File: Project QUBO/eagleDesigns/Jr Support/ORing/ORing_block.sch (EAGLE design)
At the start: 73 parts

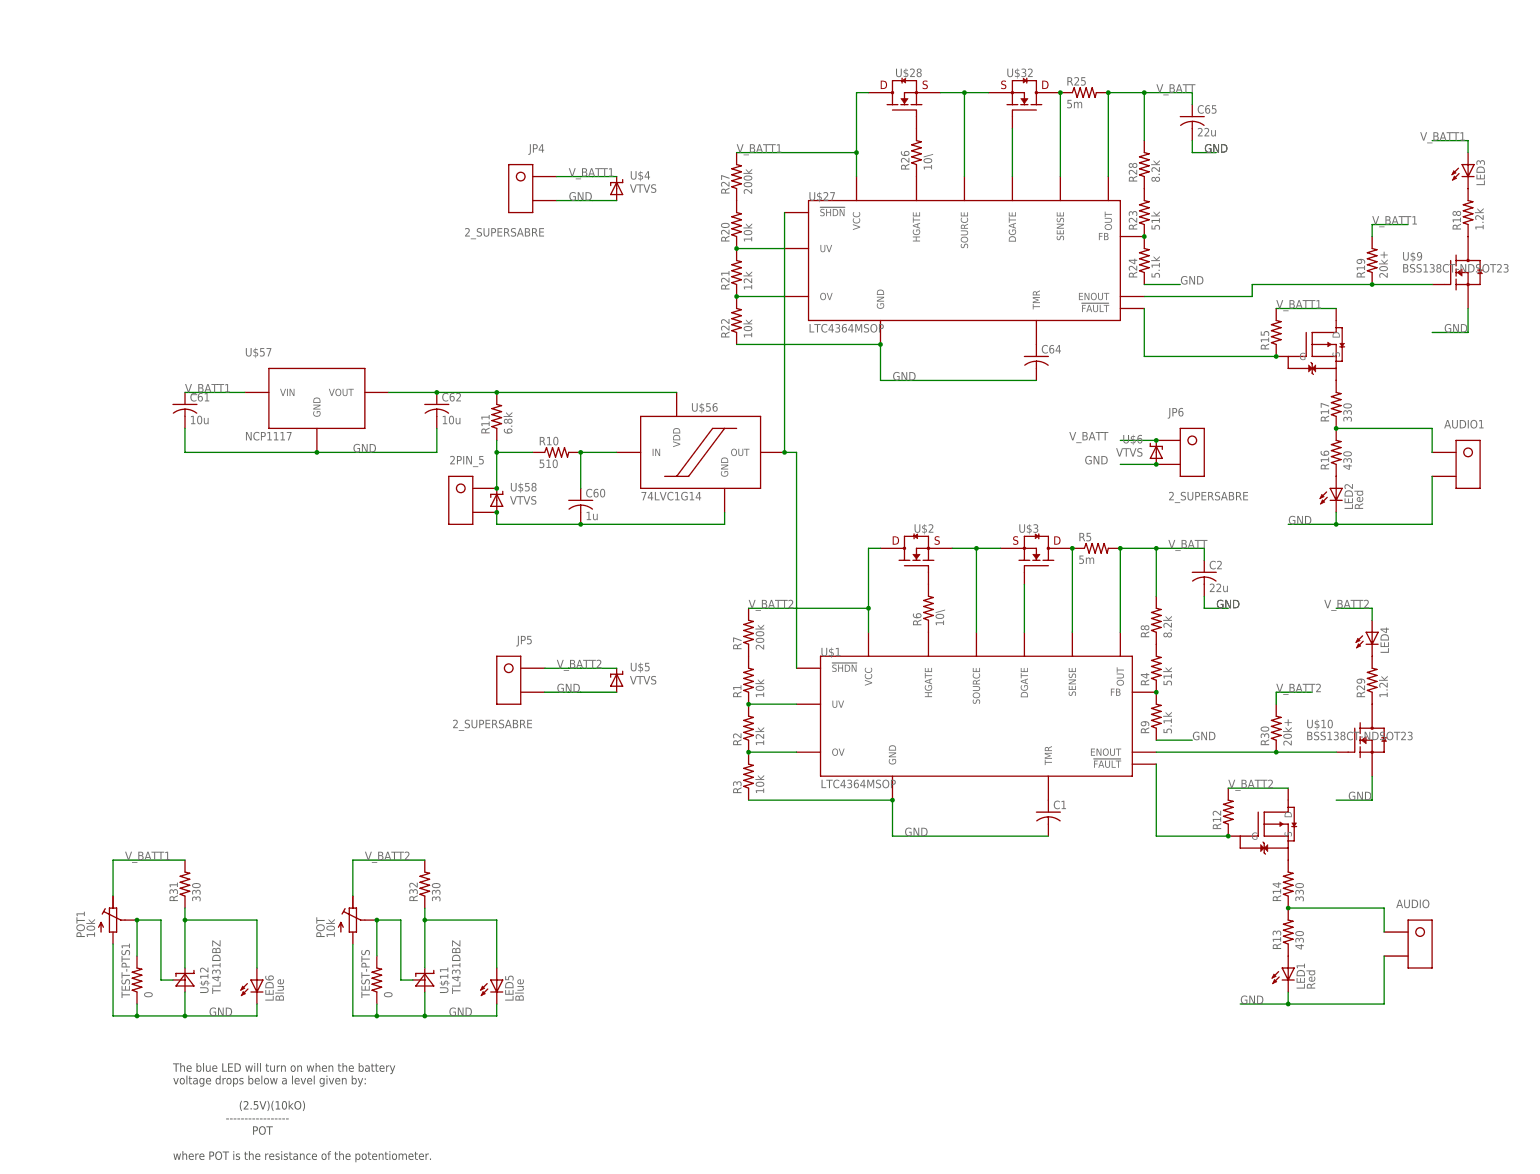
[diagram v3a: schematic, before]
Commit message: 
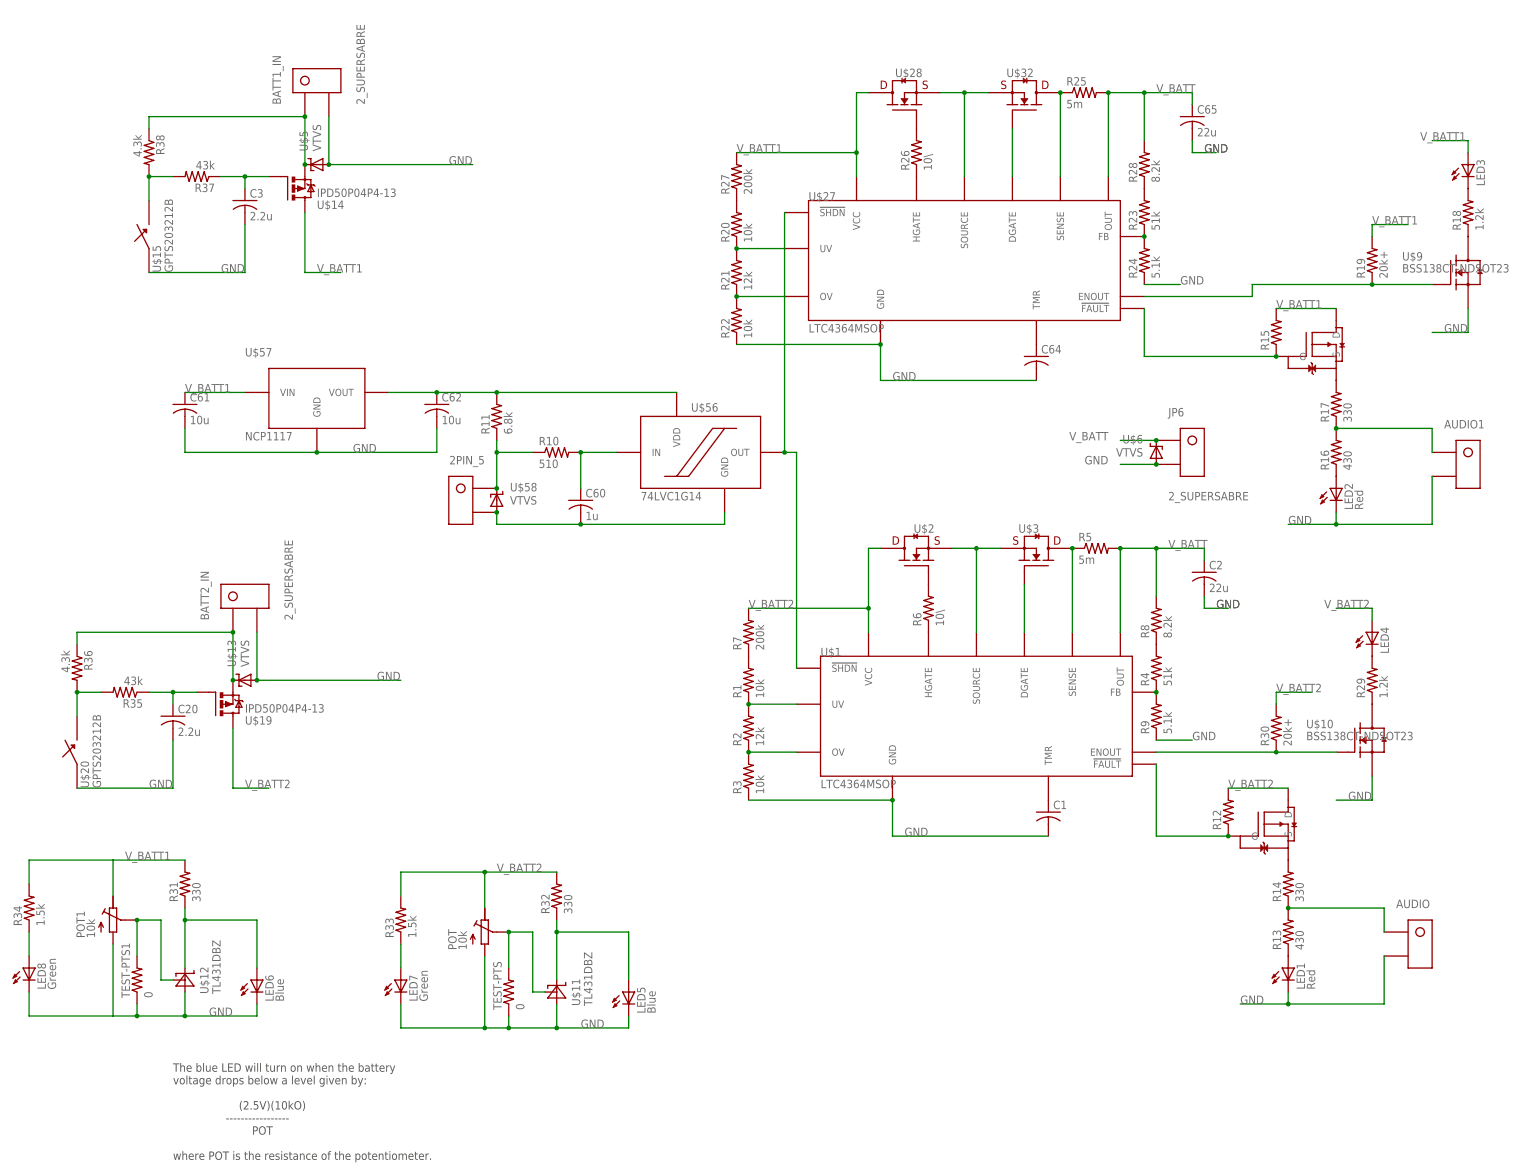
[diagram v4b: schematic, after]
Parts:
- removed JP4, JP5: 2_SUPERSABRE, molex:2_SUPERSABRE
- removed U$4: VTVS, diode:VTVS
- added BATT1_IN, BATT2_IN: 2_SUPERSABRE, molex:2_SUPERSABRE
- added C20, C3: 2.2u, resistor:C-USC0805
- added LED7, LED8: Green, led:0805_LED
- added R33, R34: 1.5k, resistor:R-US_R0805
- added R35, R37: 43k, resistor:R-US_R0805
- added R36, R38: 4.3k, resistor:R-US_R0805
- added U$13: VTVS, diode:VTVS
- added U$14, U$19: IPD50P04P4-13, transistor-power:IPD50P04P4-13
- added U$15, U$20: GPTS203212B, switches:GPTS203212B
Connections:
- new net GND1: LED8.C
- new net N$33: LED7.A, R33.1
- new net N$34: LED8.A, R34.1
- new net N$35: C20.1, R35.1, U$19.G
- new net N$36: R35.2, R36.2, U$20.P$2
- new net N$38: BATT1_IN.P$1, R38.1, U$14.D, U$5.C
- new net N$40: C3.1, R37.1, U$14.G
- new net N$41: R37.2, R38.2, U$15.P$2
- new net N$45: BATT2_IN.P$1, R36.1, U$13.C, U$19.D
- new net V_BATT3: R34.2
- net GND: now also BATT1_IN.P$2, BATT2_IN.P$2, C20.2, C3.2, LED7.C, U$13.A, U$15.P$1, U$20.P$1; no longer JP4.P$2, JP5.P$2, U$4.A
- net V_BATT1: now also U$14.S; no longer JP4.P$1, U$4.C
- net V_BATT2: now also R33.2, U$19.S; no longer JP5.P$1, U$5.C
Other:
- moved on the sheet: LED5, POT, R32, TEST-PTS, U$11, U$5

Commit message: 
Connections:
- removed net GND1: LED8.C
- removed net V_BATT3: R34.2
- net GND: now also LED8.C
- net V_BATT1: now also R34.2
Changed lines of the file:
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@@
 <label x="-157.48" y="-2.54" size="1.778" layer="95"/>
+</segment>
+<segment>
+<pinref part="LED8" gate="G$1" pin="C"/>
+<wire x1="-180.34" y1="-160.02" x2="-198.12" y2="-160.02" width="0.1524" layer="91"/>
+<wire x1="-198.12" y1="-160.02" x2="-198.12" y2="-154.94" width="0.1524" layer="91"/>
 </segment>
 </net>
@@
 <wire x1="-139.7" y1="-2.54" x2="-132.08" y2="-2.54" width="0.1524" layer="91"/>
 <label x="-137.16" y="-2.54" size="1.778" layer="95"/>
+</segment>
+<segment>
+<pinref part="R34" gate="G$1" pin="2"/>
+<wire x1="-198.12" y1="-132.08" x2="-198.12" y2="-127" width="0.1524" layer="91"/>
+<wire x1="-198.12" y1="-127" x2="-180.34" y2="-127" width="0.1524" layer="91"/>
 </segment>
 </net>
@@
 </segment>
 </net>
-<net name="GND1" class="0">
-<segment>
-<pinref part="LED8" gate="G$1" pin="C"/>
-<wire x1="-180.34" y1="-160.02" x2="-198.12" y2="-160.02" width="0.1524" layer="91"/>
-<wire x1="-198.12" y1="-160.02" x2="-198.12" y2="-154.94" width="0.1524" layer="91"/>
-</segment>
-</net>
-<net name="V_BATT3" class="0">
-<segment>
-<pinref part="R34" gate="G$1" pin="2"/>
-<wire x1="-198.12" y1="-132.08" x2="-198.12" y2="-127" width="0.1524" layer="91"/>
-<wire x1="-198.12" y1="-127" x2="-180.34" y2="-127" width="0.1524" layer="91"/>
-</segment>
-</net>

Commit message: 
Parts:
- removed R1, R20, R22, R3: 10k, resistor:R-US_R0805
- R2: value 12k -> 20.8k
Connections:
- removed net N$2: R2.1, R3.2, U$1.OV
- removed net N$47: R21.1, R22.2, U$27.OV
- removed net N$5: R1.2, R7.1
- removed net N$51: R20.2, R27.1
- net GND: now also R2.1, R21.1, U$1.OV, U$27.OV; no longer R22.1, R3.1
- net N$1: now also R7.1; no longer R1.1
- net N$39: now also R27.1; no longer R20.1
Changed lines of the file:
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@@
 <parts>
 <part name="U$27" library="linear" deviceset="LTC4364" device="MSOP"/>
-<part name="R20" library="resistor" deviceset="R-US_" device="R0805" value="10k"/>
 <part name="R21" library="resistor" deviceset="R-US_" device="R0805" value="12k"/>
-<part name="R22" library="resistor" deviceset="R-US_" device="R0805" value="10k"/>
 <part name="R23" library="resistor" deviceset="R-US_" device="R0805" value="51k"/>
 <part name="R25" library="resistor" deviceset="R-US_" device="R0805" value="5m"/>
@@
 <part name="R24" library="resistor" deviceset="R-US_" device="R0805" value="5.1k"/>
 <part name="U$1" library="linear" deviceset="LTC4364" device="MSOP"/>
-<part name="R1" library="resistor" deviceset="R-US_" device="R0805" value="10k"/>
-<part name="R2" library="resistor" deviceset="R-US_" device="R0805" value="12k"/>
-<part name="R3" library="resistor" deviceset="R-US_" device="R0805" value="10k"/>
+<part name="R2" library="resistor" deviceset="R-US_" device="R0805" value="20.8k"/>
 <part name="R4" library="resistor" deviceset="R-US_" device="R0805" value="51k"/>
 <part name="R5" library="resistor" deviceset="R-US_" device="R0805" value="5m"/>
@@
 <instances>
 <instance part="U$27" gate="G$1" x="0" y="0"/>
-<instance part="R20" gate="G$1" x="-48.26" y="7.62" rot="R90"/>
 <instance part="R21" gate="G$1" x="-48.26" y="-2.54" rot="R90"/>
-<instance part="R22" gate="G$1" x="-48.26" y="-12.7" rot="R90"/>
 <instance part="R23" gate="G$1" x="38.1" y="10.16" rot="R90"/>
 <instance part="R25" gate="G$1" x="25.4" y="35.56"/>
@@
 <instance part="R24" gate="G$1" x="38.1" y="0" rot="R90"/>
 <instance part="U$1" gate="G$1" x="2.54" y="-96.52"/>
-<instance part="R1" gate="G$1" x="-45.72" y="-88.9" rot="R90"/>
 <instance part="R2" gate="G$1" x="-45.72" y="-99.06" rot="R90"/>
-<instance part="R3" gate="G$1" x="-45.72" y="-109.22" rot="R90"/>
 <instance part="R4" gate="G$1" x="40.64" y="-86.36" rot="R90"/>
 <instance part="R5" gate="G$1" x="27.94" y="-60.96"/>
@@
 <segment>
 <pinref part="U$27" gate="G$1" pin="GND"/>
-<pinref part="R22" gate="G$1" pin="1"/>
 <wire x1="-48.26" y1="-17.78" x2="-17.78" y2="-17.78" width="0.1524" layer="91"/>
 <pinref part="C64" gate="G$1" pin="2"/>
@@
 <junction x="-17.78" y="-17.78"/>
 <label x="-15.24" y="-25.4" size="1.778" layer="95"/>
+<pinref part="R21" gate="G$1" pin="1"/>
+<pinref part="U$27" gate="G$1" pin="OV"/>
+<wire x1="-38.1" y1="-7.62" x2="-48.26" y2="-7.62" width="0.1524" layer="91"/>
+<wire x1="-48.26" y1="-7.62" x2="-48.26" y2="-17.78" width="0.1524" layer="91"/>
+<junction x="-48.26" y="-7.62"/>
 </segment>
 <segment>
@@
 <segment>
 <pinref part="U$1" gate="G$1" pin="GND"/>
-<pinref part="R3" gate="G$1" pin="1"/>
 <wire x1="-45.72" y1="-114.3" x2="-15.24" y2="-114.3" width="0.1524" layer="91"/>
 <pinref part="C1" gate="G$1" pin="2"/>
@@
 <junction x="-15.24" y="-114.3"/>
 <label x="-12.7" y="-121.92" size="1.778" layer="95"/>
+<pinref part="R2" gate="G$1" pin="1"/>
+<pinref part="U$1" gate="G$1" pin="OV"/>
+<wire x1="-35.56" y1="-104.14" x2="-45.72" y2="-104.14" width="0.1524" layer="91"/>
+<wire x1="-45.72" y1="-104.14" x2="-45.72" y2="-114.3" width="0.1524" layer="91"/>
+<junction x="-45.72" y="-104.14"/>
 </segment>
 <segment>
@@
 <net name="N$39" class="0">
 <segment>
-<pinref part="R20" gate="G$1" pin="1"/>
 <pinref part="R21" gate="G$1" pin="2"/>
 <pinref part="U$27" gate="G$1" pin="UV"/>
 <wire x1="-38.1" y1="2.54" x2="-48.26" y2="2.54" width="0.1524" layer="91"/>
+<pinref part="R27" gate="G$1" pin="1"/>
+<wire x1="-48.26" y1="12.7" x2="-48.26" y2="2.54" width="0.1524" layer="91"/>
 <junction x="-48.26" y="2.54"/>
-</segment>
-</net>
-<net name="N$47" class="0">
-<segment>
-<pinref part="R21" gate="G$1" pin="1"/>
-<pinref part="R22" gate="G$1" pin="2"/>
-<pinref part="U$27" gate="G$1" pin="OV"/>
-<wire x1="-38.1" y1="-7.62" x2="-48.26" y2="-7.62" width="0.1524" layer="91"/>
-<junction x="-48.26" y="-7.62"/>
 </segment>
 </net>
@@
 <pinref part="U$27" gate="G$1" pin="HGATE"/>
 <pinref part="R26" gate="G$1" pin="1"/>
-</segment>
-</net>
-<net name="N$51" class="0">
-<segment>
-<pinref part="R20" gate="G$1" pin="2"/>
-<pinref part="R27" gate="G$1" pin="1"/>
 </segment>
 </net>
@@
 <net name="N$1" class="0">
 <segment>
-<pinref part="R1" gate="G$1" pin="1"/>
 <pinref part="R2" gate="G$1" pin="2"/>
 <pinref part="U$1" gate="G$1" pin="UV"/>
 <wire x1="-35.56" y1="-93.98" x2="-45.72" y2="-93.98" width="0.1524" layer="91"/>
+<pinref part="R7" gate="G$1" pin="1"/>
+<wire x1="-45.72" y1="-83.82" x2="-45.72" y2="-93.98" width="0.1524" layer="91"/>
 <junction x="-45.72" y="-93.98"/>
-</segment>
-</net>
-<net name="N$2" class="0">
-<segment>
-<pinref part="R2" gate="G$1" pin="1"/>
-<pinref part="R3" gate="G$1" pin="2"/>
-<pinref part="U$1" gate="G$1" pin="OV"/>
-<wire x1="-35.56" y1="-104.14" x2="-45.72" y2="-104.14" width="0.1524" layer="91"/>
-<junction x="-45.72" y="-104.14"/>
 </segment>
 </net>
@@
 </segment>
 </net>
-<net name="N$5" class="0">
-<segment>
-<pinref part="R1" gate="G$1" pin="2"/>
-<pinref part="R7" gate="G$1" pin="1"/>
-</segment>
-</net>
